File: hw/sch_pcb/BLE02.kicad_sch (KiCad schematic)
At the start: 26 parts, among them J1 Conn_Coaxial, J2 3.3-5V, M1 HOLE, M2 HOLE, M3 HOLE, M4 HOLE, U5 CC2564CRVMR, Y3 ECS-260-8-36CKM-TR

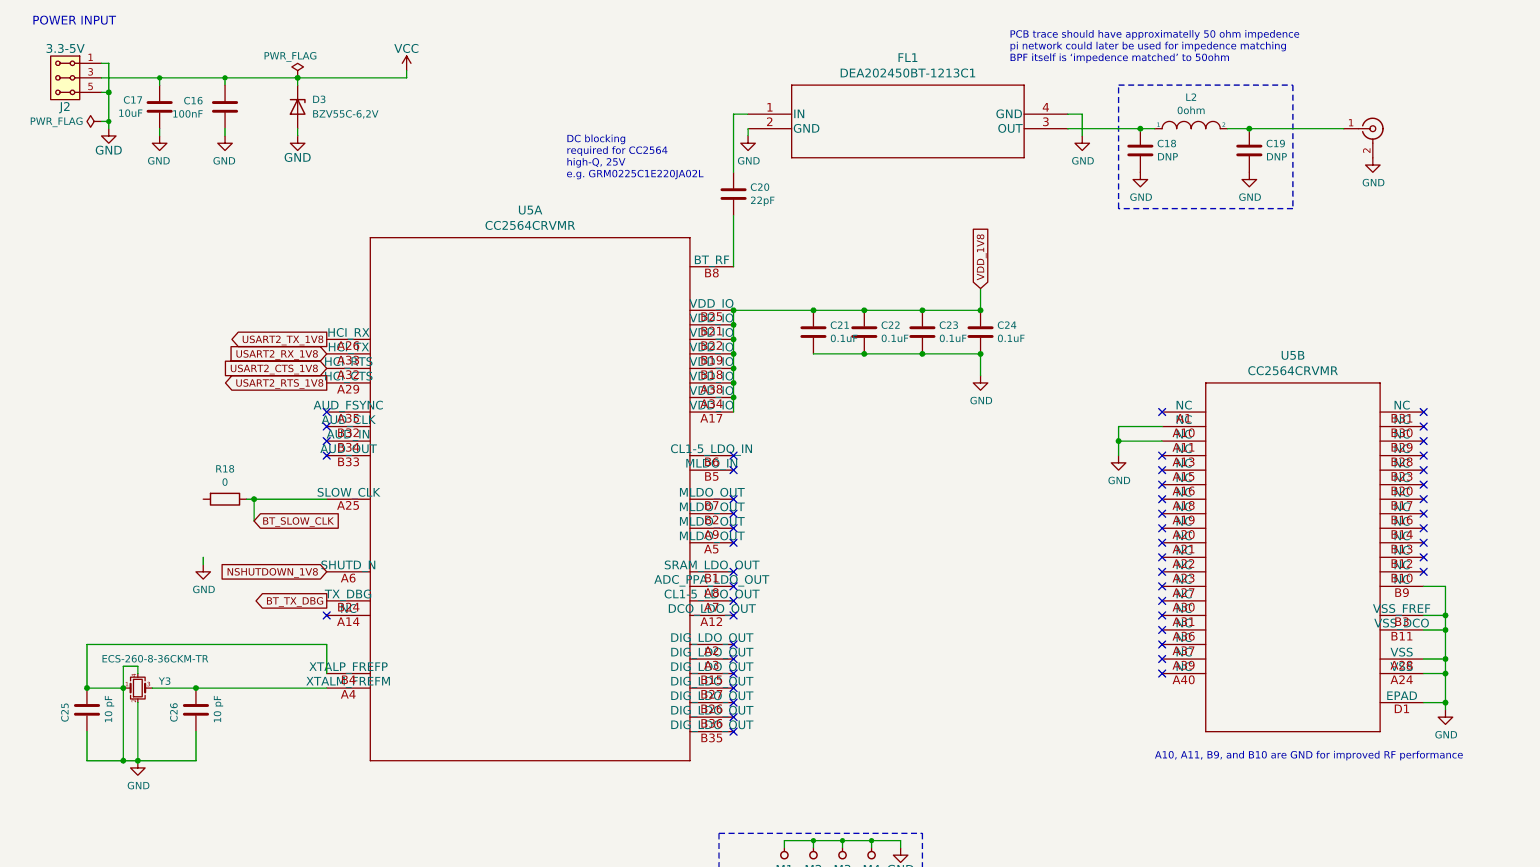
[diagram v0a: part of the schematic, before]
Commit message: Connectors placement on the board
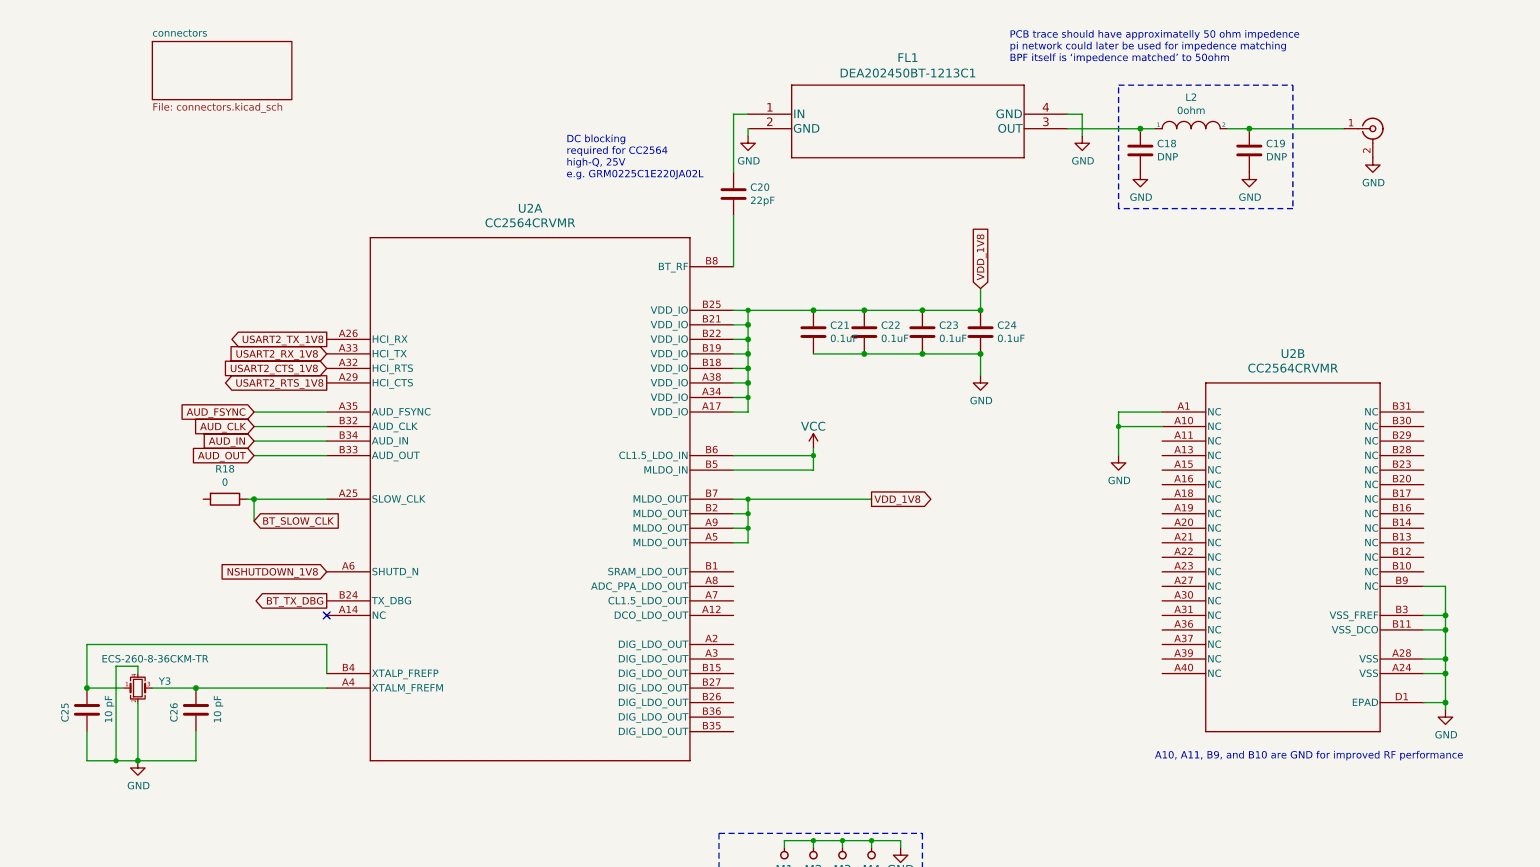
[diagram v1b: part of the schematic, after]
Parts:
- removed C16: 100nF, Capacitor_SMD:C_0805_2012Metric, symbol Device:C
- removed C17: 10uF, Capacitor_SMD:C_0805_2012Metric, symbol Device:C
- removed D3: BZV55C-6,2V, Diode_SMD:D_MiniMELF, symbol Device:D_Zener
- removed J2: 3.3-5V, Mlab_Pin_Headers:Straight_2x03, symbol MLAB_HEADER:HEADER_2x03_PARALLEL
- removed U5: CC2564CRVMR, cc2654-board-footprints:CC2564CRVMR, symbol TI-CC2564:CC2564CRVMR
- added U2: CC2564CRVMR, MLAB_Lib:RVM0076A, symbol MLAB_Lib:CC2564CRVMR
- C18, C19, C20, C21, C22, C23, C24, C25, C26: footprint Capacitor_SMD:C_0402_1005Metric_Pad0.74x0.62mm_HandSolder -> Capacitor_SMD:C_0603_1608Metric
- L2: footprint Inductor_SMD:L_0402_1005Metric_Pad0.77x0.64mm_HandSolder -> Capacitor_SMD:C_0603_1608Metric
- R18: footprint Resistor_SMD:R_0402_1005Metric_Pad0.72x0.64mm_HandSolder -> Resistor_SMD:R_0603_1608Metric
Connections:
- net BT_SLOW_CLK: now also U2.A25 (SLOW_CLK)
- net BT_TX_DBG: now also U2.B24 (TX_DBG)
- net GND: now also U2.A1 (NC), U2.A10 (NC), U2.A24 (VSS), U2.A28 (VSS), U2.B11 (VSS_DCO), U2.B3 (VSS_FREF), U2.B9 (NC), U2.D1 (EPAD); no longer C25.2, Y3.1
- net NSHUTDOWN_1V8: now also U2.A6 (SHUTD_N)
- net USART2_CTS_1V8: now also U2.A32 (HCI_RTS)
- net USART2_RTS_1V8: now also U2.A29 (HCI_CTS)
- net USART2_RX_1V8: now also U2.A33 (HCI_TX)
- net USART2_TX_1V8: now also U2.A26 (HCI_RX)
- net VCC: now also U2.B5 (MLDO_IN), U2.B6 (CL1.5_LDO_IN)
- net VDD_1V8: now also U2.A17 (VDD_IO), U2.A34 (VDD_IO), U2.A38 (VDD_IO), U2.A5 (MLDO_OUT), U2.A9 (MLDO_OUT), U2.B18 (VDD_IO), U2.B19 (VDD_IO), U2.B2 (MLDO_OUT), U2.B21 (VDD_IO), U2.B22 (VDD_IO), U2.B25 (VDD_IO), U2.B7 (MLDO_OUT)
- net at C26.2, Y3.3: now also U2.A4 (XTALM_FREFM)
- net at C20.2: now also U2.B8 (BT_RF)
- new net: C25.2, U2.B4 (XTALP_FREFP), Y3.1
- new net AUD_CLK: U2.B32 (AUD_CLK)
- new net AUD_FSYNC: U2.A35 (AUD_FSYNC)
- new net AUD_IN: U2.B34 (AUD_IN)
- new net AUD_OUT: U2.B33 (AUD_OUT)
- no-connect marks 51 -> 1
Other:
- added sheet connectors (connectors.kicad_sch)
- note removed: "POWER INPUT"

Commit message: Update project workflows.
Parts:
- C18, C19, L2: now not fitted
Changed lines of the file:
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@@
 		(exclude_from_sim no)
 		(in_bom yes)
-		(on_board yes)
-		(dnp no)
+		(on_board no)
+		(dnp yes)
 		(property "Reference" "C18"
 			(at 215.011 43.2816 0)
@@
 					(size 1.27 1.27)
 				)
+			)
+		)
+		(property "UST_ID" ""
+			(at 212.09 44.45 0)
+			(effects
+				(font
+					(size 1.27 1.27)
+				)
+				(hide yes)
 			)
 		)
@@
 		(exclude_from_sim no)
 		(in_bom yes)
-		(on_board yes)
-		(dnp no)
+		(on_board no)
+		(dnp yes)
 		(property "Reference" "C19"
 			(at 234.061 43.2816 0)
@@
 					(size 1.27 1.27)
 				)
+			)
+		)
+		(property "UST_ID" ""
+			(at 231.14 44.45 0)
+			(effects
+				(font
+					(size 1.27 1.27)
+				)
+				(hide yes)
 			)
 		)
@@
 		(exclude_from_sim no)
 		(in_bom yes)
-		(on_board yes)
-		(dnp no)
+		(on_board no)
+		(dnp yes)
 		(property "Reference" "L2"
 			(at 220.98 35.179 0)
@@
 			)
 		)
+		(property "UST_ID" ""
+			(at 220.98 40.64 0)
+			(effects
+				(font
+					(size 1.27 1.27)
+				)
+				(hide yes)
+			)
+		)

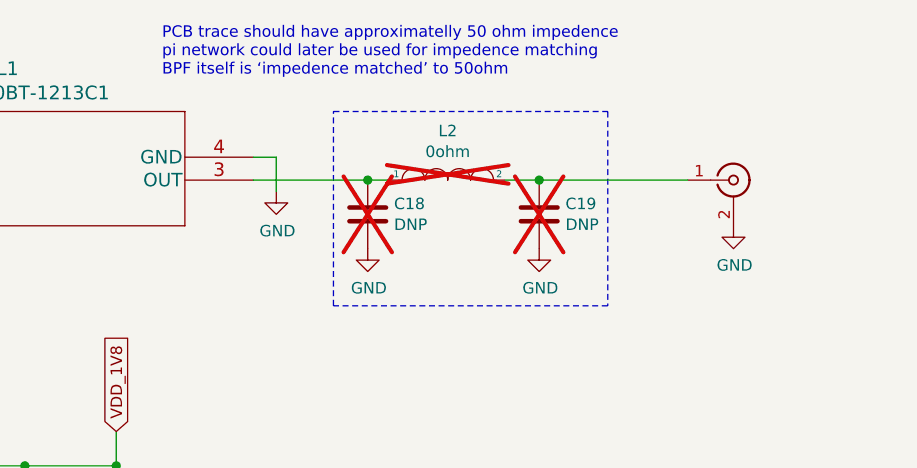
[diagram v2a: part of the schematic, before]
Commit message: Fix footprint of pin-headers.
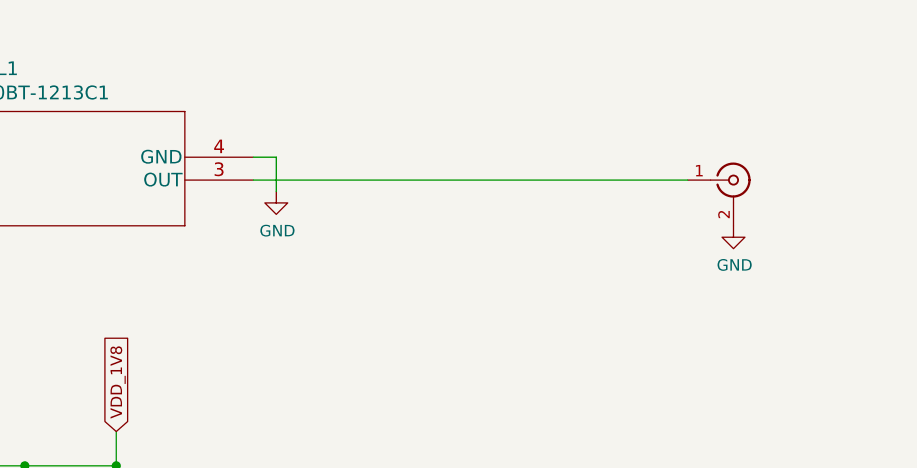
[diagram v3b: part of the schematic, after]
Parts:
- removed C18, C19: DNP, Capacitor_SMD:C_0603_1608Metric, symbol cc2564-board-rescue:C-Device
- removed L2: 0ohm, Capacitor_SMD:C_0603_1608Metric, symbol cc2564-board-rescue:INDUCTOR-pspice
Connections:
- net at FL1.3 (OUT): now also J1.1 (In)
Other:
- note removed: "PCB trace should have approximatelly 50 ohm impedence pi network could later be used for impedence matching BPF itself is ‘impedence matched’ to 50ohm"

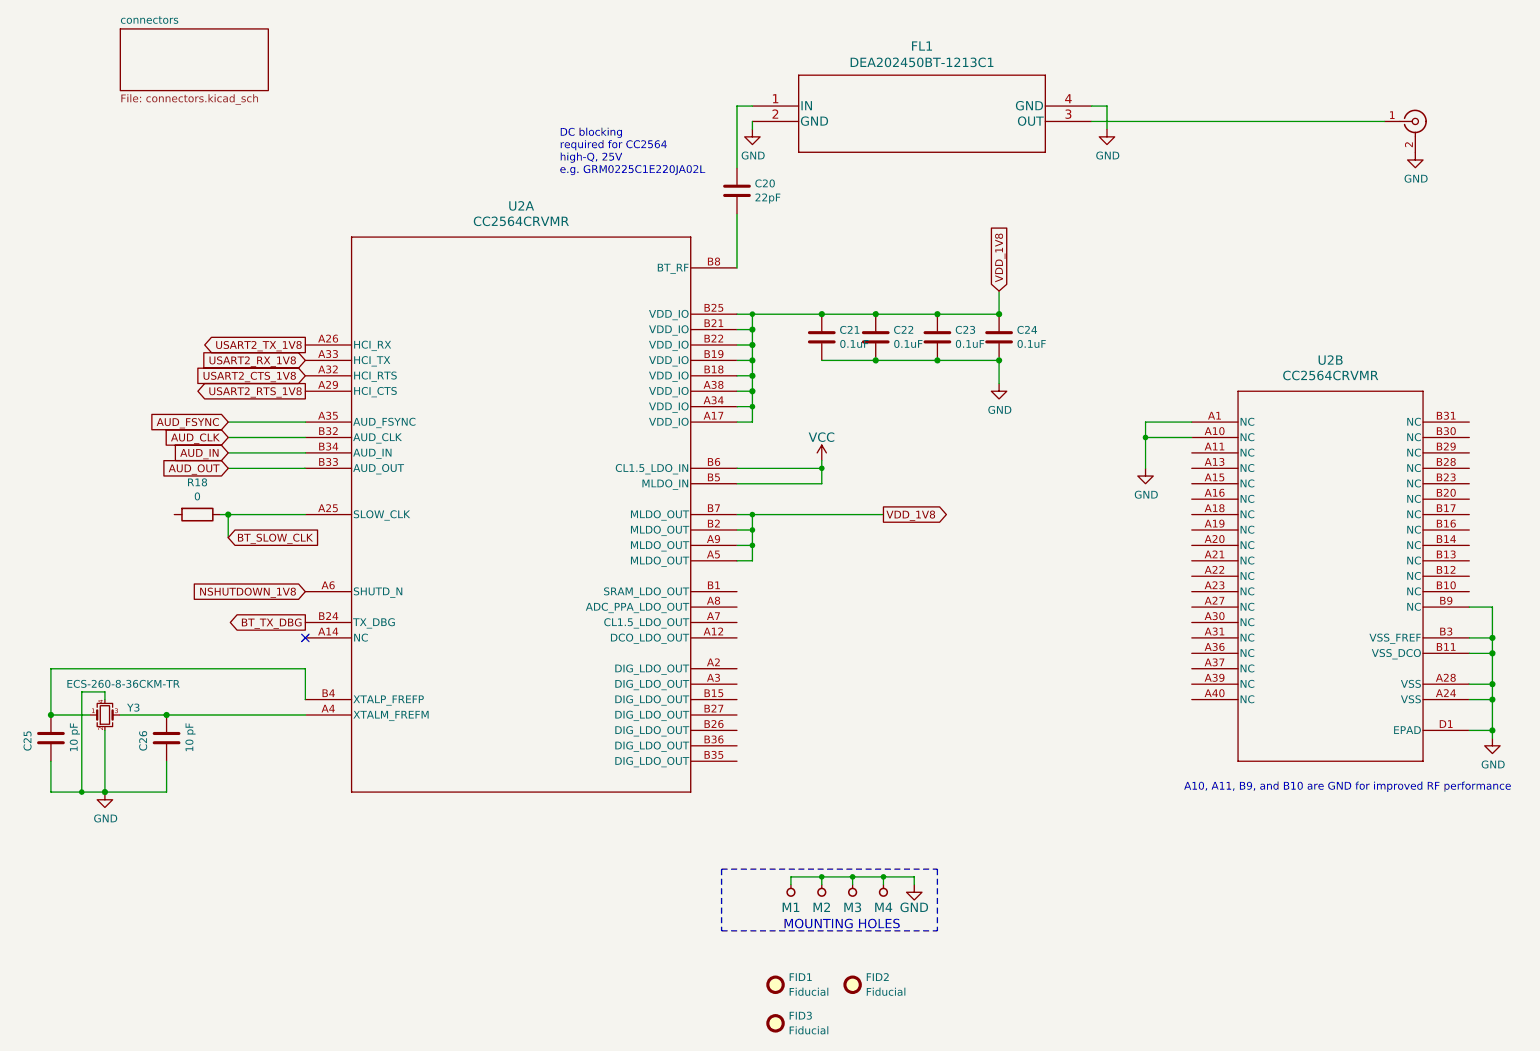
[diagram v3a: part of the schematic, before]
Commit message: Add text for connectors
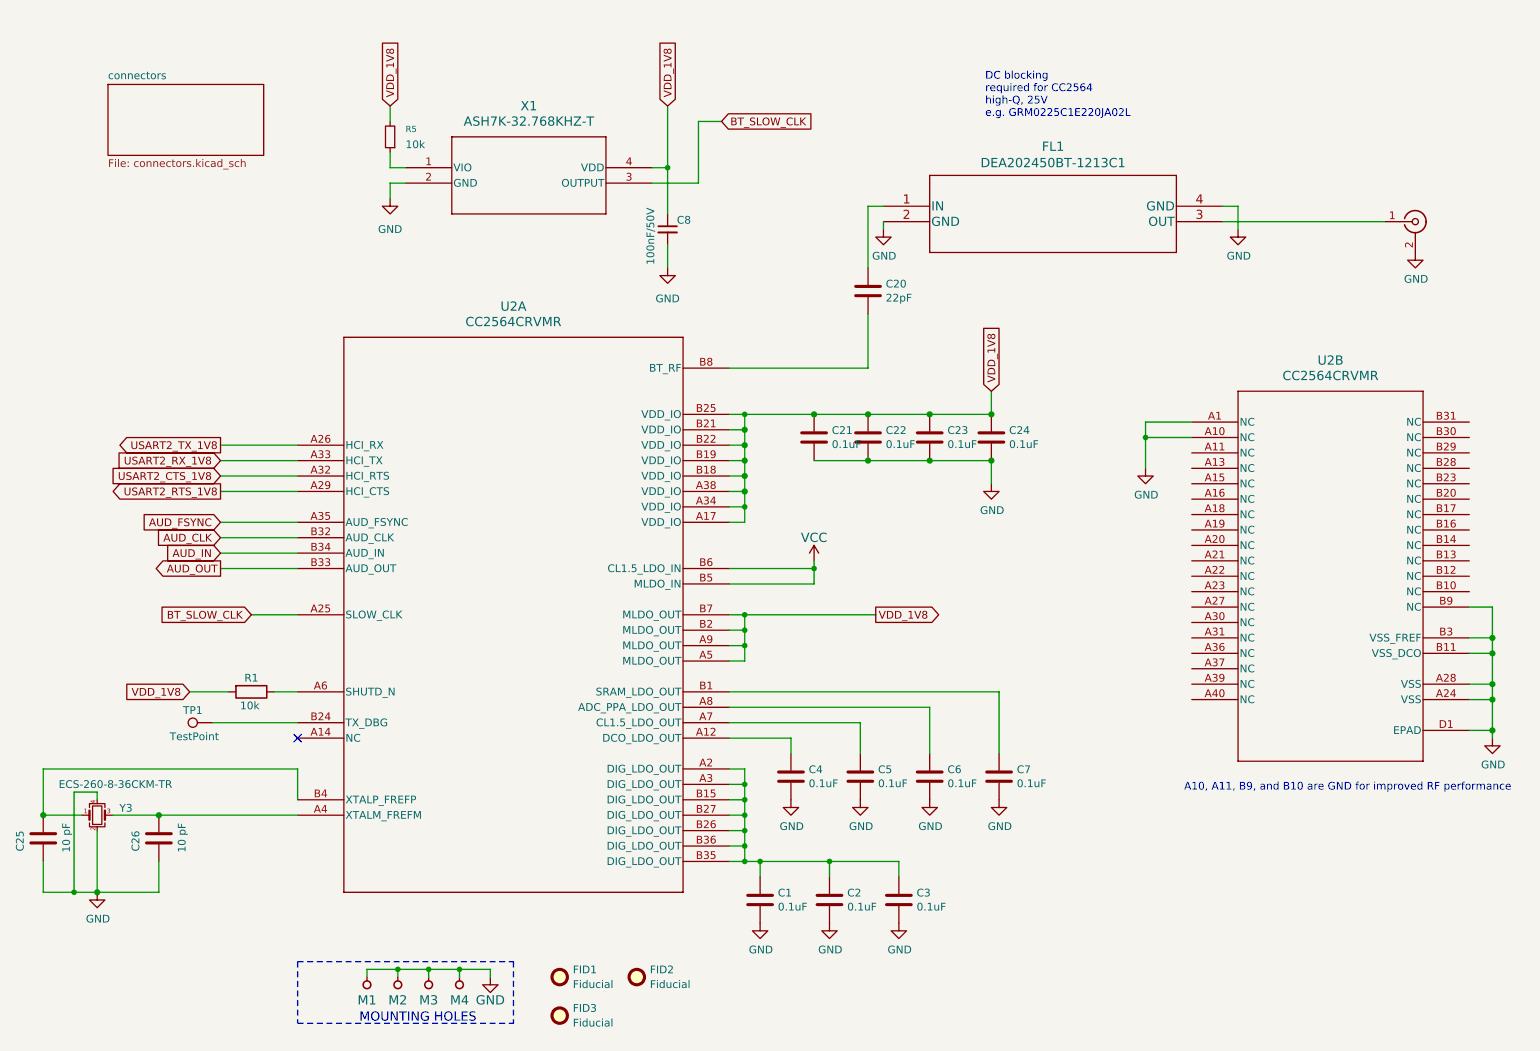
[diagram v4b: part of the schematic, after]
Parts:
- removed R18: 0, Resistor_SMD:R_0603_1608Metric, symbol cc2564-board-rescue:R-Device
- added C1, C2, C3, C4, C5, C6, C7: 0.1uF, Capacitor_SMD:C_0603_1608Metric, symbol cc2564-board-rescue:C-Device
- added C8: 100nF/50V, Capacitor_SMD:C_0603_1608Metric_Pad1.08x0.95mm_HandSolder, symbol Device:C_Small
- added R1: 10k, Resistor_SMD:R_0603_1608Metric, symbol cc2564-board-rescue:R-Device
- added R5: 10k, Resistor_SMD:R_0603_1608Metric_Pad0.98x0.95mm_HandSolder, symbol Device:R_Small
- added TP1: TestPoint, TestPoint:TestPoint_Pad_D1.0mm, symbol Connector:TestPoint
- added X1: ASH7K-32.768KHZ-T, ASH7K_ABR, symbol MLAB_Lib:ASH7K-32.768KHZ-T
- U2: footprint MLAB_Lib:RVM0076A -> RVM0076A
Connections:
- net BT_SLOW_CLK: now also X1.3 (OUTPUT)
- net GND: now also C1.2, C2.2, C3.2, C4.2, C5.2, C6.2, C7.2, C8.2, X1.2 (GND)
- net VDD_1V8: now also C8.1, R1.2, R5.2, X1.4 (VDD)
- net at U2.A12 (DCO_LDO_OUT): now also C4.1
- net at U2.A2 (DIG_LDO_OUT): now also U2.A3 (DIG_LDO_OUT), U2.B15 (DIG_LDO_OUT), U2.B26 (DIG_LDO_OUT), U2.B27 (DIG_LDO_OUT), U2.B35 (DIG_LDO_OUT), U2.B36 (DIG_LDO_OUT), C1.1, C2.1, C3.1
- net at U2.A7 (CL1.5_LDO_OUT): now also C5.1
- net at U2.A8 (ADC_PPA_LDO_OUT): now also C6.1
- net at U2.B1 (SRAM_LDO_OUT): now also C7.1
- net BT_TX_DBG: no longer names the net of U2.B24 (TX_DBG)
- net BT_TX_DBG: now also TP1.1
- net NSHUTDOWN_1V8: no longer names the net of U2.A6 (SHUTD_N)
- net NSHUTDOWN_1V8: now also R1.1
- new net: R5.1, X1.1 (VIO)
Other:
- moved on the sheet: C20, C21, C22, C23, C24, C25, C26, FID1, FID2, FID3, FL1, M1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

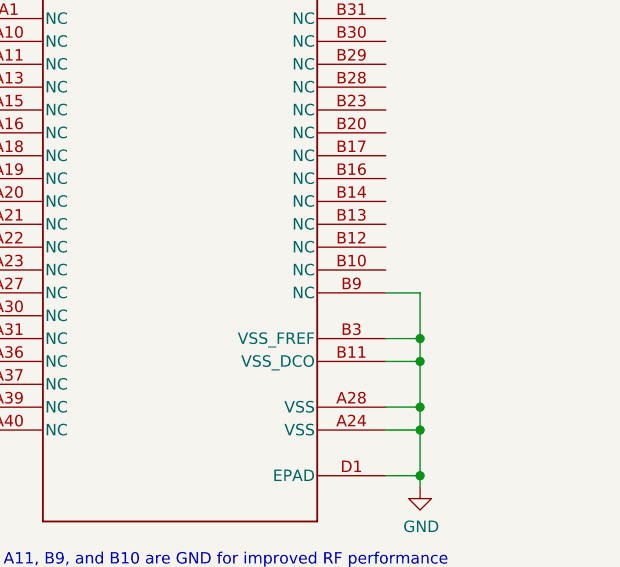
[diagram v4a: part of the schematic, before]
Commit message: Connect B10 to gnd
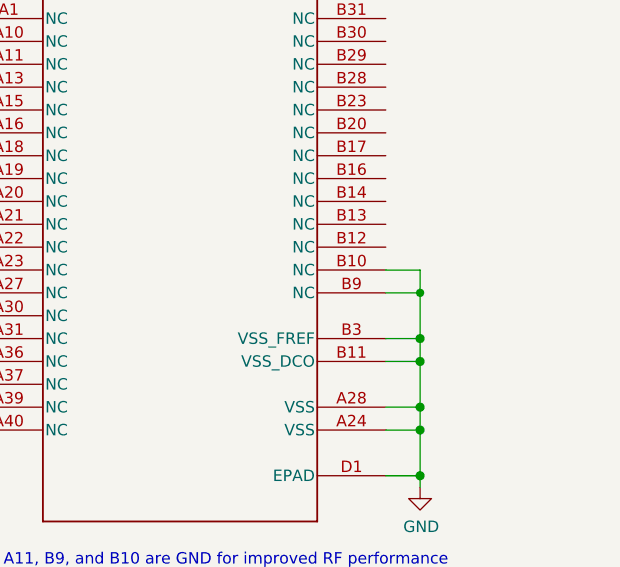
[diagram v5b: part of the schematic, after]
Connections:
- net GND: now also U2.B10 (NC)
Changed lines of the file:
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@@
+	)
+	(junction
+		(at 265.43 120.65)
+		(diameter 0)
+		(color 0 0 0 0)
 	)
 	(junction
@@
 	(wire
 		(pts
+			(xy 261.62 118.11) (xy 265.43 118.11)
+		)
+		(stroke
+			(width 0)
+			(type default)
+		)
+	)
+	(wire
+		(pts
 			(xy 142.24 157.48) (xy 142.24 160.02)
 		)
@@
 		)
 		(stroke
+			(width 0)
+			(type default)
+		)
+	)
+	(wire
+		(pts
+			(xy 265.43 118.11) (xy 265.43 120.65)
+		)
+		(stroke
